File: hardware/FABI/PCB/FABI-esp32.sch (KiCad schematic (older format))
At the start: 93 parts, among them J1 PJ320D, J10 Conn_01x06, J11 PJ320D, J12 Conn_01x08, J13 tp, J14 tp, J15 tp, J16 tp, J17 tp, J2 PJ320D, J3 PJ320D, J4 PJ320D, J5 PJ320D, J6 PJ320D, J7 PJ320D, J8 Conn_01x04, J9 USB_OTG, Q1 BC847, Q2 BSH108, Q3 BC847, Q4 BSH108, Q5 BSH108, Q6 BSH108, SW1 SW_Push, U1 ESP32-WROOM, U3 LPC11U14FBD, U4 TSR 1 (0.5) -2433, Y1 JA-12.000-18-DFE

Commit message: PCB updates: -) Changed TVS diodes to same array as used for USB -) modified part positions to avoid courtyard errors -) Modified SK6812 circuit (use diode to reduce supply voltage of led -> drivable with 3v3 signals)
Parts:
- removed D1, D2, D3, D4, D5, D6, D7: PESD3V3C1BSFYL, Diodes_SMD:D_0603, symbol D_Zener_ALT
- removed D14, D15, D8: NNCD5.6C-T1-A, Diodes_SMD:D_0603, symbol D_Zener_ALT
- removed J1, J11, J2, J3, J4, J5, J6, J7: PJ320D, Connect:PJ320D_3.5mm_Jack, symbol Audio-Jack-4
- removed J12: Conn_01x08, Pin_Headers:Pin_Header_Straight_1x08_Pitch2.54mm, symbol Conn_01x08
- removed JP1: IO direct, Resistors_SMD:R_0402_NoSilk, symbol Jumper_NO_Small
- removed Q6: BSH108, TO_SOT_Packages_SMD:SOT-23, symbol Q_NMOS_GSD
- removed R14: 1k, Resistors_SMD:R_0603, symbol R
- removed U4: TSR 1 (0.5) -2433, TO_SOT_Packages_THT:TO-220_Vertical, symbol LF33_TO220
- added D1, D2, D3: IP4220CZ6,125, SOT457:SOT457, symbol ip4220cz6,125:IP4220CZ6,125
- added D4: 1N4148WS, Diode_SMD:D_SOD-323, symbol Device:D
- added J1, J11, J2, J3, J4, J5, J6, J7: PJ320D, Connector_Audio:Jack_3.5mm_PJ320D_Horizontal, symbol Connector:Conn_01x04_Female
- added J12: Conn_01x08_Male, Connector_PinHeader_2.54mm:PinHeader_1x08_P2.54mm_Vertical, symbol Connector:Conn_01x08_Male
- added U4: TSR_1-2433, Converter_DCDC:Converter_DCDC_TRACO_TSR-1_THT, symbol Regulator_Switching:TSR_1-2433
- BZ1: footprint Buzzers_Beepers:MagneticBuzzer_Kingstate_KCG0601 -> Buzzer_Beeper:MagneticBuzzer_Kingstate_KCG0601; symbol Buzzer -> FABI-esp32-rescue:Buzzer
- C1, C11, C12, C14, C17, C18, C2, C20, C21, C22, C23, C3, C4, C5, C6, C7, C8, C9: footprint Capacitors_SMD:C_0603 -> Capacitor_SMD:C_0603_1608Metric; symbol C -> FABI-esp32-rescue:C
- C10, C13, C15, C19: footprint Capacitors_SMD:C_0805 -> Capacitor_SMD:C_0805_2012Metric; symbol C -> FABI-esp32-rescue:C
- C16: value 100uF -> 15uF; footprint Capacitors_Tantalum_SMD:CP_Tantalum_Case-A_EIA-3216-18_Reflow -> Capacitor_Tantalum_SMD:CP_EIA-3216-18_Kemet-A; symbol CP -> FABI-esp32-rescue:CP; RS-components (none) -> 699-2841
- D11: symbol SK6812 -> LED1:SK6812
- D9: symbol IP4220CZ6,125 -> ip4220cz6,125:IP4220CZ6,125
- F1: footprint Capacitors_SMD:C_1206_HandSoldering -> Capacitor_SMD:C_1206_3216Metric; symbol Polyfuse_Small -> FABI-esp32-rescue:Polyfuse_Small
- J10: footprint Pin_Headers:Pin_Header_Straight_1x06_Pitch2.54mm -> Connector_PinHeader_2.54mm:PinHeader_1x06_P2.54mm_Vertical; symbol Conn_01x06 -> FABI-esp32-rescue:Conn_01x06
- J13, J14, J15, J16, J17: footprint Measurement_Points:Measurement_Point_Round-SMD-Pad_Small -> TestPoint:TestPoint_Pad_D1.0mm; symbol TEST_1P -> FABI-esp32-rescue:TEST_1P
- J8: footprint Pin_Headers:Pin_Header_Straight_1x04_Pitch2.54mm -> Connector_PinSocket_2.54mm:PinSocket_1x04_P2.54mm_Vertical; symbol Conn_01x04 -> FABI-esp32-rescue:Conn_01x04
- J9: symbol USB_OTG -> FABI-esp32-rescue:USB_OTG
- L1: footprint Capacitors_SMD:C_0805_HandSoldering -> Inductor_SMD:L_0805_2012Metric; symbol L_Core_Ferrite_Small -> FABI-esp32-rescue:L_Core_Ferrite_Small
- Q1, Q3: footprint TO_SOT_Packages_SMD:SOT-23 -> Package_TO_SOT_SMD:SOT-23; symbol BC847 -> FABI-esp32-rescue:BC847
- Q2, Q4, Q5: footprint TO_SOT_Packages_SMD:SOT-23 -> Package_TO_SOT_SMD:SOT-23; symbol Q_NMOS_GSD -> FABI-esp32-rescue:Q_NMOS_GSD
- R1, R10, R11, R12, R13, R15, R16, R17, R18, R19, R2, R20, R21, R22, R3, R4, R5, R6, R7, R8, R9: footprint Resistors_SMD:R_0603 -> Resistor_SMD:R_0603_1608Metric; symbol R -> FABI-esp32-rescue:R
- SW1: symbol SW_Push -> FABI-esp32-rescue:SW_Push
- TP1, TP2, TP3, TP4: footprint Mounting_Holes:MountingHole_4.5mm -> MountingHole:MountingHole_4.5mm; symbol TEST -> FABI-esp32-rescue:TEST
- U1: symbol ESP32-WROOM -> ESP32-footprints-Shem-Lib:ESP32-WROOM
- U3: footprint Housings_QFP:LQFP-48_7x7mm_Pitch0.5mm -> Package_QFP:LQFP-48_7x7mm_P0.5mm; symbol LPC11U14FBD -> LPC11:LPC11U14FBD
- Y1: footprint Crystals:Crystal_SMD_3225-4pin_3.2x2.5mm -> Crystal:Crystal_SMD_3225-4Pin_3.2x2.5mm; symbol Crystal_GND24 -> FABI-esp32-rescue:Crystal_GND24
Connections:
- net labels added: DD+, DD-
- wire segments 172 -> 235
- no-connect marks 66 -> 52
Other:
- note added: "Note: to have 3v3 compatible SK6812,\nwe need to reduce the supply voltage:\n5V-0,7V->4,3V*0,7->Din(high,min) = 3V"
- note removed: "Pinning for PJ-320:\n1: Tip\n2: 2nd ring\n4: 3rd ring\n3: base ring\n(3/4 changed)"
- note removed: "SoftConnect"
- note removed: "compatible to \nLPCXpresso 11U14"
- note removed: "route 3v3 directly\nto Neopixel"
- moved on the sheet: C1, C10, C2, C3, C4, C5, C7, C9, J10, J16, J17, Q1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

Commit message: Finalized FABI PCB, added PDFs & finalized BOM
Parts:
- added FID1, FID2, FID3: Fiducial, Fiducial:Fiducial_0.5mm_Dia_1mm_Outer, symbol Mechanical:MountingHole
- added LOGO1: LOGO_CE, Logo:CE, symbol Mechanical:MountingHole
- added LOGO2, LOGO4: LOGO_FABI, Logo:fabi_15x8, symbol Mechanical:MountingHole
- added LOGO3: LOGO_WEEE, Symbol:WEEE-Logo_4.2x6mm_SilkScreen, symbol Mechanical:MountingHole
- MH1: renamed from TP1; footprint MountingHole:MountingHole_4.5mm -> Mount:MountingHole_4.5mm_wo_crtyd
- MH2: renamed from TP2; footprint MountingHole:MountingHole_4.5mm -> Mount:MountingHole_4.5mm_wo_crtyd
- MH3: renamed from TP3; footprint MountingHole:MountingHole_4.5mm -> Mount:MountingHole_4.5mm_wo_crtyd
- MH4: renamed from TP4; footprint MountingHole:MountingHole_4.5mm -> Mount:MountingHole_4.5mm_wo_crtyd
- renumbered C6 to C1, C14 to C10, C18 to C12, C20 to C13, C21 to C14, C23 to C15, C22 to C16, C12 to C18, C8 to C2, C13 to C20, C10 to C21, C15 to C22, C16 to C23, C1 to C6, C2 to C8, D9 to D4, D4 to D5, D11 to D6, J8 to J10, J10 to J11, J11 to J8, Q3 to Q2, Q2 to Q3, R15 to R1, R17 to R11, R2 to R12, R1 to R14, R22 to R15, R21 to R16, R11 to R17, R16 to R2, R12 to R21, R8 to R4, R4 to R8, U4 to U2
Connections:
- net BUZZER: now also U1.12 (IO27); no longer U1.13 (IO14)
- net B_6: now also U1.13 (IO14); no longer U1.12 (IO27)
- net GNDD: now also J2.2 (Pin_2), J2.3 (Pin_3), J3.2 (Pin_2), J3.3 (Pin_3), J4.2 (Pin_2), J4.3 (Pin_3), J5.2 (Pin_2), J5.3 (Pin_3), J6.2 (Pin_2), J6.3 (Pin_3), J7.2 (Pin_2), J7.3 (Pin_3)
- net SCL: now also U3.15 (PIO0_4/SCL)
- net SDA: now also U3.16 (PIO0_5/SDA)
- no-connect marks 52 -> 50
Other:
- note added: "Fiducials"
- note added: "Infrared (external)"
- note added: "Logos"
- note added: "Microcontrollers"
- note added: "Power"
- note added: "Production"
- note added: "USB compatible interface"
- note added: "User I/O\n"
- moved on the sheet: BZ1, C1, C10, C11, C12, C13, C14, C15, C16, C17, C18, C19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

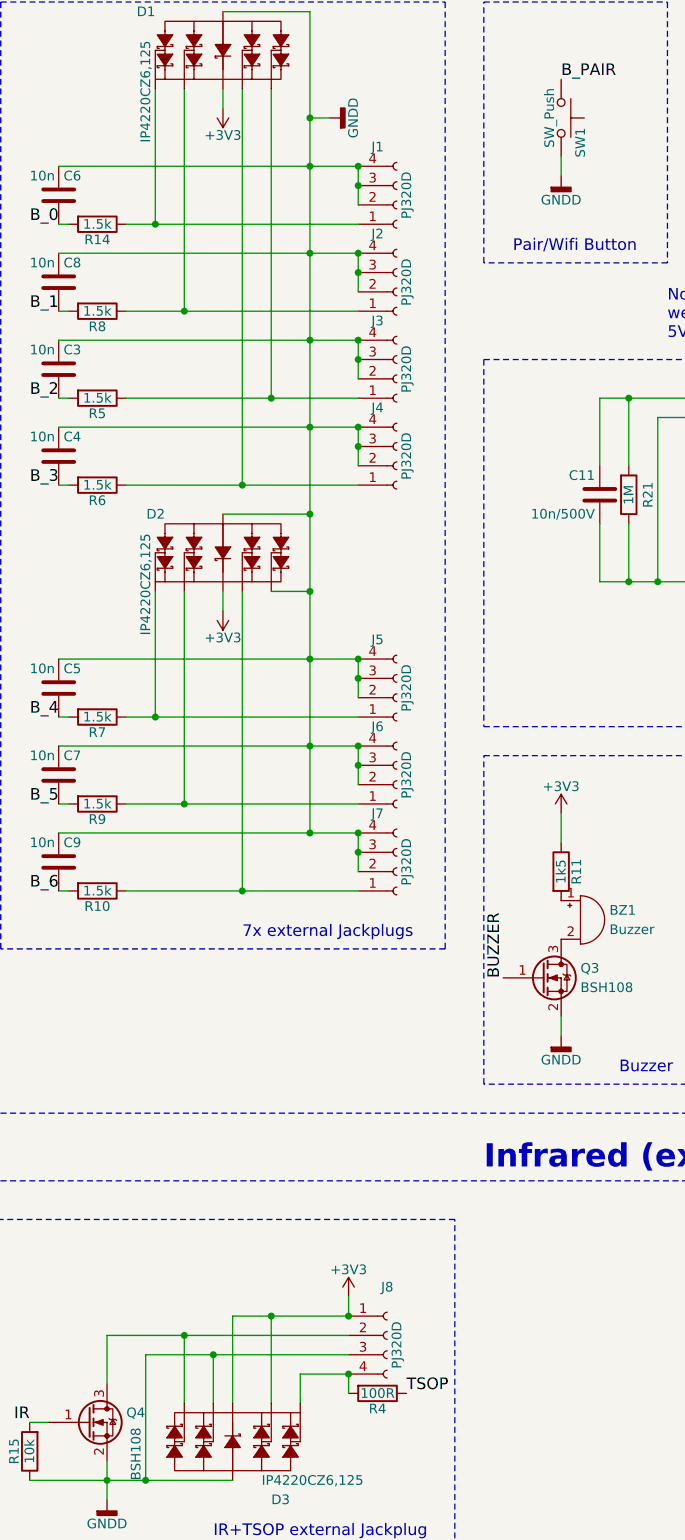
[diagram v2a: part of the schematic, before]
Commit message: 3D cleanup, should be now ready for production
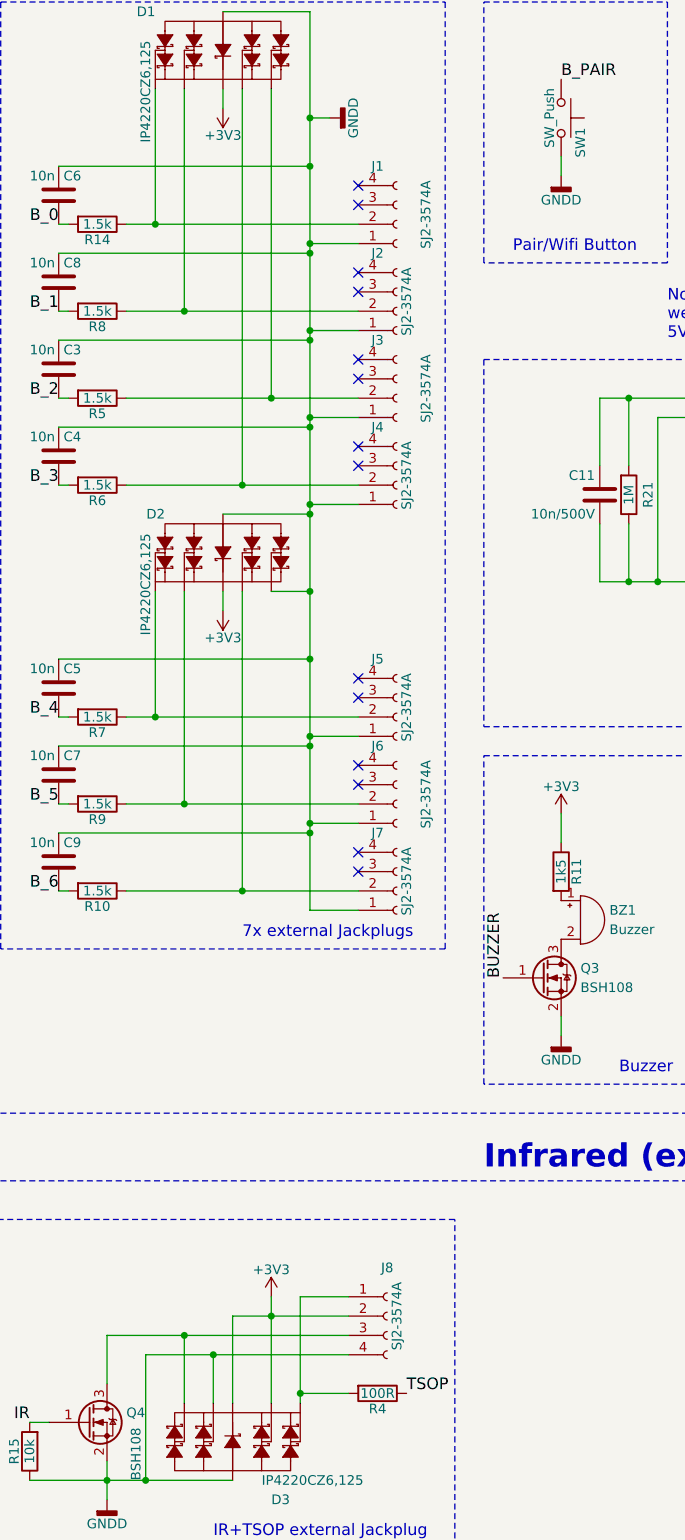
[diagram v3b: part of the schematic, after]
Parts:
- J1, J2, J3, J4, J5, J6, J7, J8: value PJ320D -> SJ2-3574A; footprint Connector_Audio:Jack_3.5mm_PJ320D_Horizontal -> JackPlug:Jack_3.5mm_SJ2-357X
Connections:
- net +3V3: now also J8.2 (Pin_2); no longer J8.1 (Pin_1)
- net GNDD: now also J1.1 (Pin_1), J2.1 (Pin_1), J3.1 (Pin_1), J4.1 (Pin_1), J5.1 (Pin_1), J6.1 (Pin_1), J7.1 (Pin_1), J8.4 (Pin_4); no longer J1.2 (Pin_2), J1.3 (Pin_3), J1.4 (Pin_4), J2.2 (Pin_2), J2.3 (Pin_3), J2.4 (Pin_4), J3.2 (Pin_2), J3.3 (Pin_3), J3.4 (Pin_4), J4.2 (Pin_2), J4.3 (Pin_3), J4.4 (Pin_4), J5.2 (Pin_2), J5.3 (Pin_3), J5.4 (Pin_4), J6.2 (Pin_2), J6.3 (Pin_3), J6.4 (Pin_4), J7.2 (Pin_2), J7.3 (Pin_3), J7.4 (Pin_4), J8.3 (Pin_3)
- net at D1.4 (IO), R8.1: now also J2.2 (Pin_2); no longer J2.1 (Pin_1)
- net at D1.1 (IO), R5.1: now also J3.2 (Pin_2); no longer J3.1 (Pin_1)
- net at D1.3 (IO), R6.1: now also J4.2 (Pin_2); no longer J4.1 (Pin_1)
- net at D1.6 (IO), R14.1: now also J1.2 (Pin_2); no longer J1.1 (Pin_1)
- net at D2.6 (IO), R7.1: now also J5.2 (Pin_2); no longer J5.1 (Pin_1)
- net at D2.4 (IO), R9.1: now also J6.2 (Pin_2); no longer J6.1 (Pin_1)
- net at D2.3 (IO), R10.1: now also J7.2 (Pin_2); no longer J7.1 (Pin_1)
- net at D3.6 (IO), R4.2: now also J8.1 (Pin_1); no longer J8.4 (Pin_4)
- net at D3.1 (IO), Q4.3 (D): now also J8.3 (Pin_3); no longer J8.2 (Pin_2)
- no-connect marks 50 -> 64
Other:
- moved on the sheet: J1, J2, J3, J4, J5, J6, J7, J8
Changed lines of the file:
@@
 L power:+3V3 #PWR029
 U 1 1 5A8510CA
-P 11100 7650
-F 0 "#PWR029" H 11100 7500 50  0001 C CNN
-F 1 "+3V3" H 11100 7790 50  0000 C CNN
-F 2 "" H 11100 7650 50  0001 C CNN
-F 3 "" H 11100 7650 50  0001 C CNN
-	1    11100 7650
+P 10700 7650
+F 0 "#PWR029" H 10700 7500 50  0001 C CNN
+F 1 "+3V3" H 10700 7790 50  0000 C CNN
+F 2 "" H 10700 7650 50  0001 C CNN
+F 3 "" H 10700 7650 50  0001 C CNN
+	1    10700 7650
 	1    0    0    -1
 $EndComp
@@
 NoConn ~ 7350 5350
 $Comp
-L Connector:Conn_01x04_Female J1
-U 1 1 5BF34C92
-P 11350 2000
-F 0 "J1" H 11250 1700 50  0000 C CNN
-F 1 "PJ320D" V 11400 1950 50  0000 C CNN
-F 2 "Connector_Audio:Jack_3.5mm_PJ320D_Horizontal" H 11350 2000 50  0001 C CNN
-F 3 "~" H 11350 2000 50  0001 C CNN
-	1    11350 2000
-	1    0    0    1
-$EndComp
-$Comp
 L Connector:Conn_01x04_Female J3
 U 1 1 5BFE40DB
-P 11350 2900
-F 0 "J3" H 11250 2600 50  0000 C CNN
-F 1 "PJ320D" V 11400 2850 50  0000 C CNN
-F 2 "Connector_Audio:Jack_3.5mm_PJ320D_Horizontal" H 11350 2900 50  0001 C CNN
-F 3 "~" H 11350 2900 50  0001 C CNN
-	1    11350 2900
+P 11350 3000
+F 0 "J3" H 11250 2700 50  0000 C CNN
+F 1 "SJ2-3574A" V 11500 2950 50  0000 C CNN
+F 2 "JackPlug:Jack_3.5mm_SJ2-357X" H 11350 3000 50  0001 C CNN
+F 3 "~" H 11350 3000 50  0001 C CNN
+	1    11350 3000
 	1    0    0    1
 $EndComp
@@
 L Connector:Conn_01x04_Female J4
 U 1 1 5BFF5388
-P 11350 3350
-F 0 "J4" H 11250 3050 50  0000 C CNN
-F 1 "PJ320D" V 11400 3300 50  0000 C CNN
-F 2 "Connector_Audio:Jack_3.5mm_PJ320D_Horizontal" H 11350 3350 50  0001 C CNN
-F 3 "~" H 11350 3350 50  0001 C CNN
-	1    11350 3350
+P 11350 3450
+F 0 "J4" H 11250 3150 50  0000 C CNN
+F 1 "SJ2-3574A" V 11400 3400 50  0000 C CNN
+F 2 "JackPlug:Jack_3.5mm_SJ2-357X" H 11350 3450 50  0001 C CNN
+F 3 "~" H 11350 3450 50  0001 C CNN
+	1    11350 3450
 	1    0    0    1
 $EndComp
@@
 L Connector:Conn_01x04_Female J5
 U 1 1 5BFF538E
-P 11350 4550
-F 0 "J5" H 11250 4250 50  0000 C CNN
-F 1 "PJ320D" V 11400 4500 50  0000 C CNN
-F 2 "Connector_Audio:Jack_3.5mm_PJ320D_Horizontal" H 11350 4550 50  0001 C CNN
-F 3 "~" H 11350 4550 50  0001 C CNN
-	1    11350 4550
+P 11350 4650
+F 0 "J5" H 11250 4350 50  0000 C CNN
+F 1 "SJ2-3574A" V 11400 4600 50  0000 C CNN
+F 2 "JackPlug:Jack_3.5mm_SJ2-357X" H 11350 4650 50  0001 C CNN
+F 3 "~" H 11350 4650 50  0001 C CNN
+	1    11350 4650
 	1    0    0    1
 $EndComp
@@
 L Connector:Conn_01x04_Female J6
 U 1 1 5C006607
-P 11350 5000
-F 0 "J6" H 11250 4700 50  0000 C CNN
-F 1 "PJ320D" V 11400 4950 50  0000 C CNN
-F 2 "Connector_Audio:Jack_3.5mm_PJ320D_Horizontal" H 11350 5000 50  0001 C CNN
-F 3 "~" H 11350 5000 50  0001 C CNN
-	1    11350 5000
+P 11350 5100
+F 0 "J6" H 11250 4800 50  0000 C CNN
+F 1 "SJ2-3574A" V 11500 5050 50  0000 C CNN
+F 2 "JackPlug:Jack_3.5mm_SJ2-357X" H 11350 5100 50  0001 C CNN
+F 3 "~" H 11350 5100 50  0001 C CNN
+	1    11350 5100
 	1    0    0    1
 $EndComp
@@
 L Connector:Conn_01x04_Female J7
 U 1 1 5C00660D
-P 11350 5450
-F 0 "J7" H 11250 5150 50  0000 C CNN
-F 1 "PJ320D" V 11400 5400 50  0000 C CNN
-F 2 "Connector_Audio:Jack_3.5mm_PJ320D_Horizontal" H 11350 5450 50  0001 C CNN
-F 3 "~" H 11350 5450 50  0001 C CNN
-	1    11350 5450
+P 11350 5550
+F 0 "J7" H 11250 5250 50  0000 C CNN
+F 1 "SJ2-3574A" V 11400 5500 50  0000 C CNN
+F 2 "JackPlug:Jack_3.5mm_SJ2-357X" H 11350 5550 50  0001 C CNN
+F 3 "~" H 11350 5550 50  0001 C CNN
+	1    11350 5550
 	1    0    0    1
 $EndComp
 Wire Wire Line
-	10900 2250 10900 2700
-Wire Wire Line
-	10900 2700 10900 3150
-Wire Wire Line
-	10900 3150 10900 3600
-Wire Wire Line
-	11150 1800 10900 1800
-Wire Wire Line
-	10900 2250 11150 2250
-Wire Wire Line
-	10900 4350 10900 4800
-Wire Wire Line
-	10900 4800 10900 5250
-Wire Wire Line
-	11150 5250 10900 5250
-Wire Wire Line
-	10900 4800 11150 4800
-Wire Wire Line
-	11150 4350 10900 4350
-Wire Wire Line
-	10900 3150 11150 3150
-Wire Wire Line
-	11150 2700 10900 2700
+	10900 2250 10900 2650
+Wire Wire Line
+	10900 2700 10900 3100
+Wire Wire Line
+	10900 3150 10900 3550
+Wire Wire Line
+	10900 4350 10900 4750
+Wire Wire Line
+	10900 4800 10900 5200
 $Comp
 L Connector:Conn_01x04_Female J8
 U 1 1 5C397289
-P 11300 7850
-F 0 "J8" H 11300 8100 50  0000 C CNN
-F 1 "PJ320D" V 11350 7800 50  0000 C CNN
-F 2 "Connector_Audio:Jack_3.5mm_PJ320D_Horizontal" H 11300 7850 50  0001 C CNN
-F 3 "~" H 11300 7850 50  0001 C CNN
-	1    11300 7850
-	1    0    0    -1
-$EndComp
-Wire Wire Line
-	11100 8050 11100 8150
-Connection ~ 11100 8050
+P 11300 7750
+F 0 "J8" H 11300 8000 50  0000 C CNN
+F 1 "SJ2-3574A" V 11350 7750 50  0000 C CNN
+F 2 "JackPlug:Jack_3.5mm_SJ2-357X" H 11300 7750 50  0001 C CNN
+F 3 "~" H 11300 7750 50  0001 C CNN
+	1    11300 7750
+	1    0    0    -1
+$EndComp
 $Comp
 L Regulator_Switching:TSR_1-2433 U2
@@
 $EndComp
 Wire Wire Line
-	11100 7650 11100 7750
-Wire Wire Line
 	9850 7850 10250 7850
 Wire Wire Line
@@
 Wire Wire Line
 	10500 7750 10700 7750
-Connection ~ 11100 7750
 Wire Wire Line
 	9850 7850 9850 8100
@@
 	10700 7750 11100 7750
 Wire Wire Line
-	10850 8200 10850 8050
-Wire Wire Line
-	10850 8050 11100 8050
-Wire Wire Line
-	11150 2000 11150 1900
-Connection ~ 11150 1800
-Connection ~ 11150 1900
-Wire Wire Line
-	11150 1900 11150 1800
-$Comp
-L Connector:Conn_01x04_Female J2
-U 1 1 5BFB0A62
-P 11350 2450
-F 0 "J2" H 11250 2150 50  0000 C CNN
-F 1 "PJ320D" V 11400 2400 50  0000 C CNN
-F 2 "Connector_Audio:Jack_3.5mm_PJ320D_Horizontal" H 11350 2450 50  0001 C CNN
-F 3 "~" H 11350 2450 50  0001 C CNN
-	1    11350 2450
-	1    0    0    1
-$EndComp
+	10850 8200 10850 8150
 Wire Wire Line
 	9950 2100 10100 2100
@@
 	9600 3150 10900 3150
 Wire Wire Line
-	10900 1800 10900 2250
-Wire Wire Line
 	9950 5550 10550 5550
 Wire Wire Line
 	9600 5250 10900 5250
-Connection ~ 10900 5250
 Wire Wire Line
 	9600 4800 10900 4800
@@
 Text Label 3550 2350 0    60   ~ 0
 SDA
-Wire Wire Line
-	11150 2450 11150 2350
-Connection ~ 11150 2250
-Connection ~ 11150 2350
-Wire Wire Line
-	11150 2350 11150 2250
-Wire Wire Line
-	11150 2900 11150 2800
-Connection ~ 11150 2700
-Connection ~ 11150 2800
-Wire Wire Line
-	11150 2800 11150 2700
-Wire Wire Line
-	11150 3350 11150 3250
-Connection ~ 11150 3150
-Connection ~ 11150 3250
-Wire Wire Line
-	11150 3250 11150 3150
-Wire Wire Line
-	11150 5450 11150 5350
-Connection ~ 11150 5250
-Connection ~ 11150 5350
-Wire Wire Line
-	11150 5350 11150 5250
-Wire Wire Line
-	11150 5000 11150 4900
-Connection ~ 11150 4800
-Connection ~ 11150 4900
-Wire Wire Line
-	11150 4900 11150 4800
-Wire Wire Line
-	11150 4550 11150 4450
-Connection ~ 11150 4350
-Connection ~ 11150 4450
-Wire Wire Line
-	11150 4450 11150 4350
 $Comp
 L Graphic:Logo_Open_Hardware_Small #LOGO100
@@
 	1    0    0    -1
 $EndComp
+$Comp
+L Connector:Conn_01x04_Female J1
+U 1 1 5BF34C92
+P 11350 2100
+F 0 "J1" H 11250 1800 50  0000 C CNN
+F 1 "SJ2-3574A" V 11500 2050 50  0000 C CNN
+F 2 "JackPlug:Jack_3.5mm_SJ2-357X" H 11350 2100 50  0001 C CNN
+F 3 "~" H 11350 2100 50  0001 C CNN
+	1    11350 2100
+	1    0    0    1
+$EndComp
+$Comp
+L Connector:Conn_01x04_Female J2
+U 1 1 5BFB0A62
+P 11350 2550
+F 0 "J2" H 11250 2250 50  0000 C CNN
+F 1 "SJ2-3574A" V 11400 2500 50  0000 C CNN
+F 2 "JackPlug:Jack_3.5mm_SJ2-357X" H 11350 2550 50  0001 C CNN
+F 3 "~" H 11350 2550 50  0001 C CNN
+	1    11350 2550
+	1    0    0    1
+$EndComp
+Wire Wire Line
+	11150 2650 10900 2650
+Connection ~ 10900 2650
+Wire Wire Line
+	10900 2650 10900 2700
+Wire Wire Line
+	10900 1800 10900 2200
+Wire Wire Line
+	11150 2200 10900 2200
+Wire Wire Line
+	11150 3100 10900 3100
+Wire Wire Line
+	11150 3550 10900 3550
+Connection ~ 10900 2200
+Wire Wire Line
+	10900 2200 10900 2250
+Connection ~ 10900 3550
+Wire Wire Line
+	10900 3550 10900 3600
+Wire Wire Line
+	11150 4750 10900 4750
+Wire Wire Line
+	11150 5200 10900 5200
+Wire Wire Line
+	11150 5650 10900 5650
+Wire Wire Line
+	10900 5650 10900 5250
+Connection ~ 10900 5250
+Connection ~ 10900 5200
+Wire Wire Line
+	10900 5200 10900 5250
+Connection ~ 10900 4750
+Wire Wire Line
+	10900 4750 10900 4800
+NoConn ~ 11150 5450
+NoConn ~ 11150 5350
+NoConn ~ 11150 5000
+NoConn ~ 11150 4900
+NoConn ~ 11150 4550
+NoConn ~ 11150 4450
+NoConn ~ 11150 3350
+NoConn ~ 11150 3250
+Connection ~ 10900 3100
+Wire Wire Line
+	10900 3100 10900 3150
+NoConn ~ 11150 2800
+NoConn ~ 11150 2900
+NoConn ~ 11150 2450
+NoConn ~ 11150 2350
+NoConn ~ 11150 2000
+NoConn ~ 11150 1900
+Wire Wire Line
+	10700 7650 10700 7750
+Wire Wire Line
+	11100 8150 10850 8150
+Connection ~ 10850 8150
+Wire Wire Line
+	10850 7650 11100 7650
+Wire Wire Line
+	10850 7650 10850 8150
 $EndSCHEMATC

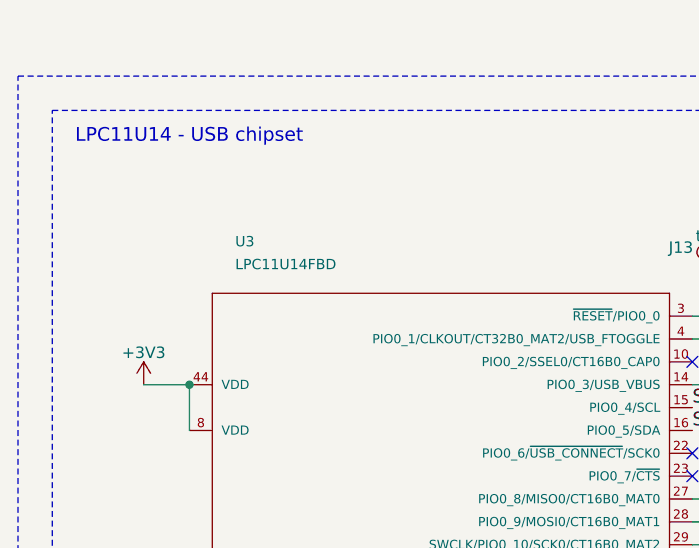
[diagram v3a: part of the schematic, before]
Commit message: Changed USB chipset to LPC11U__2__4 (from LPC11U14): This introduces the possibility to use the USB-MSD bootloader for software updates. Otherwise we would need either a serial adapter, a custom bootloader or a programming software within the ESP32 (and more nets between these two chips).
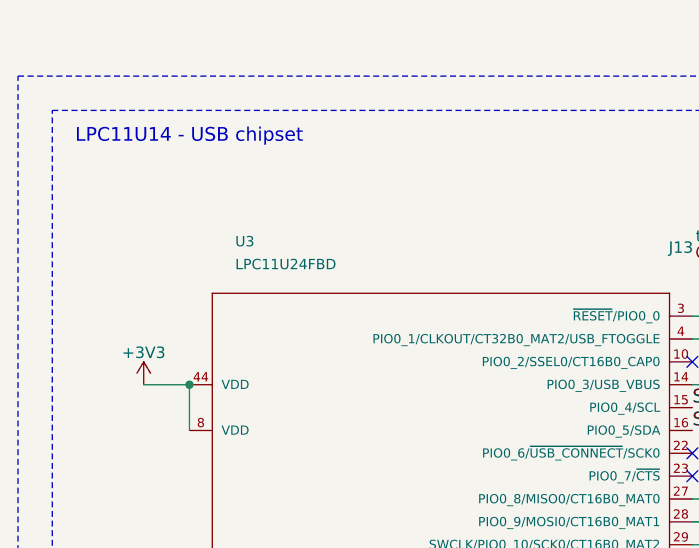
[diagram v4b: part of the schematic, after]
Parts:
- U3: value LPC11U14FBD -> LPC11U24FBD
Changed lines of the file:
@@
 P 2450 4050
 F 0 "U3" H 1550 6550 45  0000 L BNN
-F 1 "LPC11U14FBD" H 1550 6450 45  0000 L BNN
+F 1 "LPC11U24FBD" H 1550 6450 45  0000 L BNN
 F 2 "Package_QFP:LQFP-48_7x7mm_P0.5mm" H 2480 4200 20  0001 C CNN
 F 3 "" H 2450 4050 60  0001 C CNN
